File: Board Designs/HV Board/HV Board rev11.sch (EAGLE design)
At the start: 69 parts, among them IC1 OKI-78SR-5, IC2 NE5532SOIC

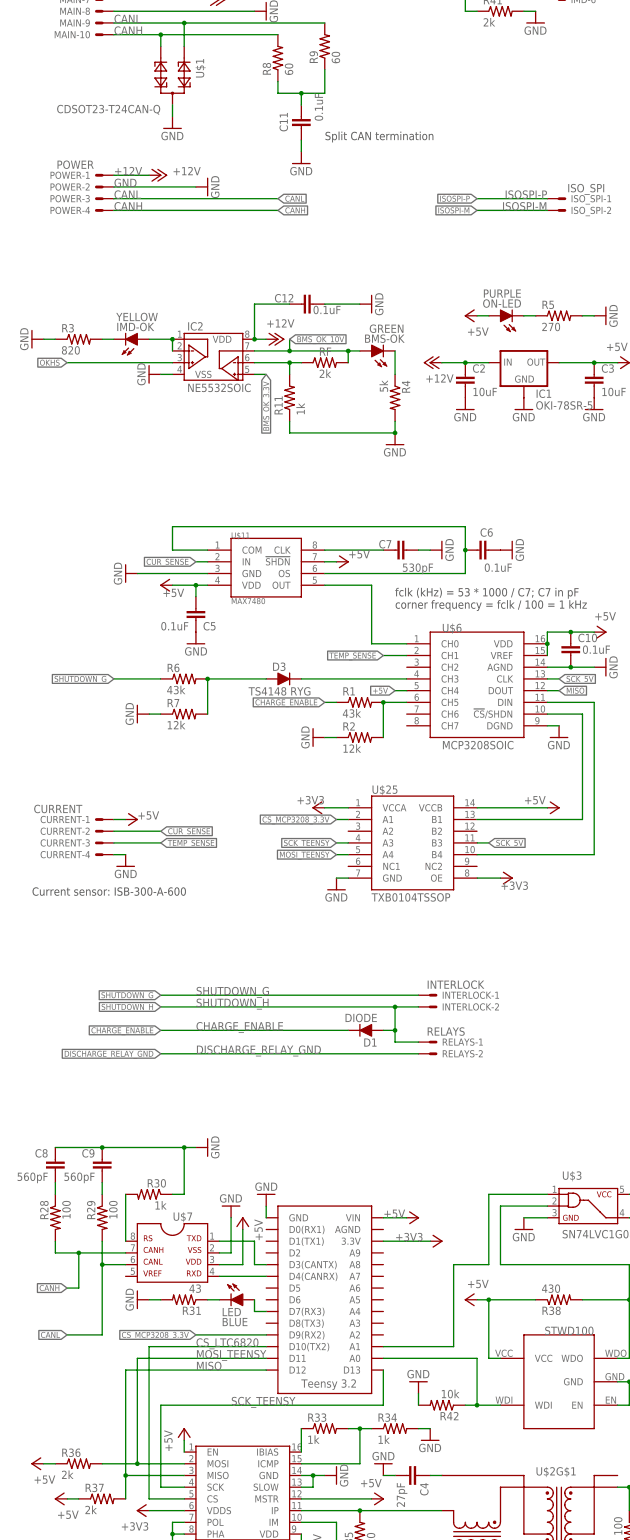
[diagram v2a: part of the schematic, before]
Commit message: HV Board: Added bypass caps to LTC6820 and SPI level shifter, rerouted under Teensy, rerouted GND/Power to 5V regulator, Silkscreen updates for mfg
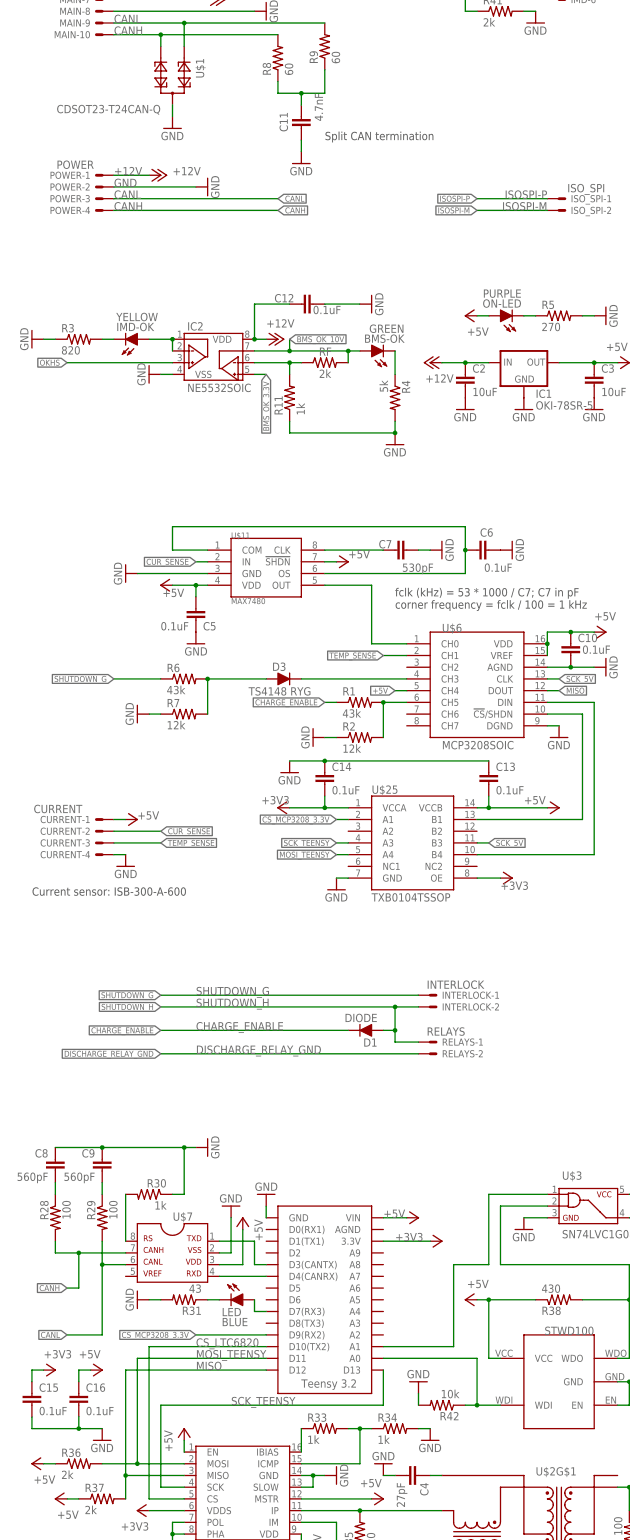
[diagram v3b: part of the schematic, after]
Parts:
- added C13, C14, C15, C16: 0.1uF, HyTechDevices:CAP0805
- C11: value 0.1uF -> 4.7nF
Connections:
- net +3V3: now also C14.1, C15.2
- net +5V: now also C13.1, C16.2
- net GND: now also C13.2, C14.2, C15.1, C16.1
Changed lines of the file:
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@@
 <part name="R8" library="HyTechDevices" deviceset="RESISTOR" device="0805-RES" value="60"/>
 <part name="R9" library="HyTechDevices" deviceset="RESISTOR" device="0805-RES" value="60"/>
-<part name="C11" library="HyTechDevices" deviceset="CAP" device="0805" value="0.1uF"/>
+<part name="C11" library="HyTechDevices" deviceset="CAP" device="0805" value="4.7nF"/>
 <part name="GND33" library="supply1" deviceset="GND" device=""/>
 <part name="RF" library="HyTechDevices" deviceset="RESISTOR" device="0805-RES" value="2k"/>
@@
 <part name="C12" library="HyTechDevices" deviceset="CAP" device="0805" value="0.1uF"/>
 <part name="GND34" library="supply1" deviceset="GND" device=""/>
+<part name="C13" library="HyTechDevices" deviceset="CAP" device="0805" value="0.1uF"/>
+<part name="C14" library="HyTechDevices" deviceset="CAP" device="0805" value="0.1uF"/>
+<part name="GND35" library="supply1" deviceset="GND" device=""/>
+<part name="C15" library="HyTechDevices" deviceset="CAP" device="0805" value="0.1uF"/>
+<part name="C16" library="HyTechDevices" deviceset="CAP" device="0805" value="0.1uF"/>
+<part name="GND36" library="HyTechSymbols" deviceset="GND" device=""/>
+<part name="P+9" library="supply1" deviceset="+5V" device=""/>
+<part name="+3V6" library="supply1" library_urn="urn:adsk.eagle:library:371" deviceset="+3V3" device=""/>
 </parts>
 <sheets>
@@
 <attribute name="VALUE" x="88.9" y="-160.02" size="1.778" layer="96"/>
 </instance>
-<instance part="+3V4" gate="G$1" x="76.2" y="-139.7" smashed="yes" rot="R90">
-<attribute name="VALUE" x="78.74" y="-137.16" size="1.778" layer="96" rot="R180"/>
+<instance part="+3V4" gate="G$1" x="68.58" y="-139.7" smashed="yes" rot="R90">
+<attribute name="VALUE" x="71.12" y="-137.16" size="1.778" layer="96" rot="R180"/>
 </instance>
 <instance part="+3V5" gate="G$1" x="119.38" y="-154.94" smashed="yes" rot="R270">
@@
 <instance part="GND34" gate="1" x="88.9" y="-30.48" smashed="yes" rot="R90">
 <attribute name="VALUE" x="91.44" y="-33.02" size="1.778" layer="96" rot="R90"/>
+</instance>
+<instance part="C13" gate="G$1" x="114.3" y="-132.08" smashed="yes" rot="MR180">
+<attribute name="NAME" x="115.824" y="-129.921" size="1.778" layer="95" rot="MR180"/>
+<attribute name="VALUE" x="115.824" y="-135.001" size="1.778" layer="96" rot="MR180"/>
+</instance>
+<instance part="C14" gate="G$1" x="78.74" y="-132.08" smashed="yes" rot="MR180">
+<attribute name="NAME" x="80.264" y="-129.921" size="1.778" layer="95" rot="MR180"/>
+<attribute name="VALUE" x="80.264" y="-135.001" size="1.778" layer="96" rot="MR180"/>
+</instance>
+<instance part="GND35" gate="1" x="71.12" y="-132.08" smashed="yes">
+<attribute name="VALUE" x="68.58" y="-134.62" size="1.778" layer="96"/>
+</instance>
+<instance part="C15" gate="G$1" x="15.24" y="-266.7" smashed="yes" rot="MR180">
+<attribute name="NAME" x="16.764" y="-264.541" size="1.778" layer="95" rot="MR180"/>
+<attribute name="VALUE" x="16.764" y="-269.621" size="1.778" layer="96" rot="MR180"/>
+</instance>
+<instance part="C16" gate="G$1" x="25.4" y="-266.7" smashed="yes" rot="MR180">
+<attribute name="NAME" x="26.924" y="-264.541" size="1.778" layer="95" rot="MR180"/>
+<attribute name="VALUE" x="26.924" y="-269.621" size="1.778" layer="96" rot="MR180"/>
+</instance>
+<instance part="GND36" gate="1" x="30.48" y="-276.86" smashed="yes">
+<attribute name="VALUE" x="27.94" y="-279.4" size="1.778" layer="96"/>
+</instance>
+<instance part="P+9" gate="1" x="30.48" y="-261.62" smashed="yes" rot="R270">
+<attribute name="VALUE" x="25.4" y="-259.08" size="1.778" layer="96"/>
+</instance>
+<instance part="+3V6" gate="G$1" x="20.32" y="-261.62" smashed="yes" rot="R270">
+<attribute name="VALUE" x="17.78" y="-259.08" size="1.778" layer="96"/>
 </instance>
 </instances>
@@
 <wire x1="78.74" y1="-30.48" x2="86.36" y2="-30.48" width="0.1524" layer="91"/>
 </segment>
+<segment>
+<pinref part="C13" gate="G$1" pin="2"/>
+<wire x1="114.3" y1="-129.54" x2="78.74" y2="-129.54" width="0.1524" layer="91"/>
+<pinref part="C14" gate="G$1" pin="2"/>
+<pinref part="GND35" gate="1" pin="GND"/>
+<wire x1="71.12" y1="-129.54" x2="78.74" y2="-129.54" width="0.1524" layer="91"/>
+<junction x="78.74" y="-129.54"/>
+</segment>
+<segment>
+<pinref part="C16" gate="G$1" pin="1"/>
+<wire x1="25.4" y1="-271.78" x2="25.4" y2="-274.32" width="0.1524" layer="91"/>
+<wire x1="25.4" y1="-274.32" x2="15.24" y2="-274.32" width="0.1524" layer="91"/>
+<pinref part="C15" gate="G$1" pin="1"/>
+<wire x1="15.24" y1="-274.32" x2="15.24" y2="-271.78" width="0.1524" layer="91"/>
+<junction x="25.4" y="-274.32"/>
+<pinref part="GND36" gate="1" pin="GND"/>
+<wire x1="30.48" y1="-274.32" x2="25.4" y2="-274.32" width="0.1524" layer="91"/>
+</segment>
 </net>
 <net name="+12V" class="0">
@@
 </segment>
 <segment>
-<wire x1="111.76" y1="-139.7" x2="127" y2="-139.7" width="0.1524" layer="91"/>
+<wire x1="111.76" y1="-139.7" x2="114.3" y2="-139.7" width="0.1524" layer="91"/>
 <pinref part="FLIP" gate="1" pin="+5V"/>
 <pinref part="U$25" gate="G$1" pin="VCCB"/>
+<pinref part="C13" gate="G$1" pin="1"/>
+<wire x1="114.3" y1="-139.7" x2="127" y2="-139.7" width="0.1524" layer="91"/>
+<wire x1="114.3" y1="-137.16" x2="114.3" y2="-139.7" width="0.1524" layer="91"/>
+<junction x="114.3" y="-139.7"/>
+</segment>
+<segment>
+<pinref part="P+9" gate="1" pin="+5V"/>
+<wire x1="27.94" y1="-261.62" x2="25.4" y2="-261.62" width="0.1524" layer="91"/>
+<pinref part="C16" gate="G$1" pin="2"/>
+<wire x1="25.4" y1="-261.62" x2="25.4" y2="-264.16" width="0.1524" layer="91"/>
 </segment>
 </net>
@@
 <pinref part="U$25" gate="G$1" pin="VCCA"/>
 <pinref part="+3V4" gate="G$1" pin="+3V3"/>
+<wire x1="71.12" y1="-139.7" x2="78.74" y2="-139.7" width="0.1524" layer="91"/>
+<pinref part="C14" gate="G$1" pin="1"/>
 <wire x1="78.74" y1="-139.7" x2="83.82" y2="-139.7" width="0.1524" layer="91"/>
+<wire x1="78.74" y1="-137.16" x2="78.74" y2="-139.7" width="0.1524" layer="91"/>
+<junction x="78.74" y="-139.7"/>
 </segment>
 <segment>
@@
 <wire x1="116.84" y1="-154.94" x2="111.76" y2="-154.94" width="0.1524" layer="91"/>
 </segment>
-</net>
+<segment>
+<pinref part="+3V6" gate="G$1" pin="+3V3"/>
+<wire x1="17.78" y1="-261.62" x2="15.24" y2="-261.62" width="0.1524" layer="91"/>
+<pinref part="C15" gate="G$1" pin="2"/>
+<wire x1="15.24" y1="-261.62" x2="15.24" y2="-264.16" width="0.1524" layer="91"/>
+</segment>
+</net>

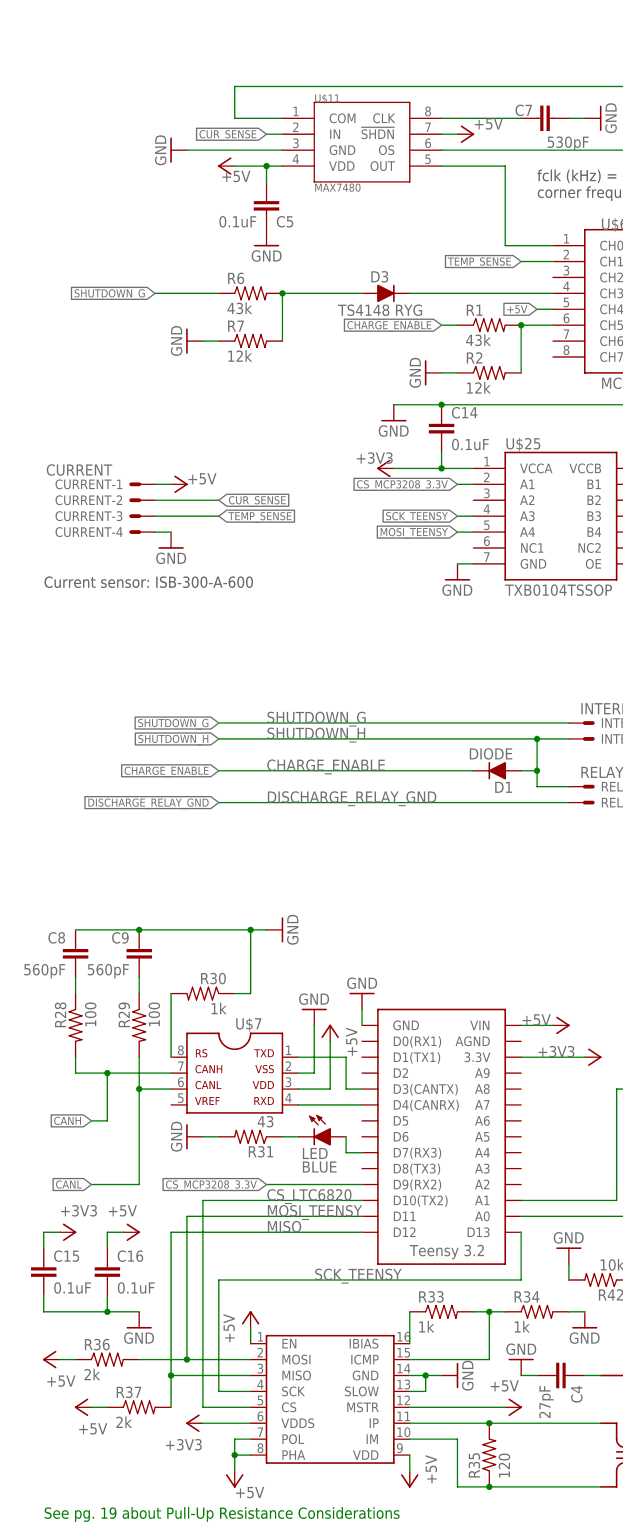
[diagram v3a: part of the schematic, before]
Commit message: Final version of HV board rev11 sent for mfg
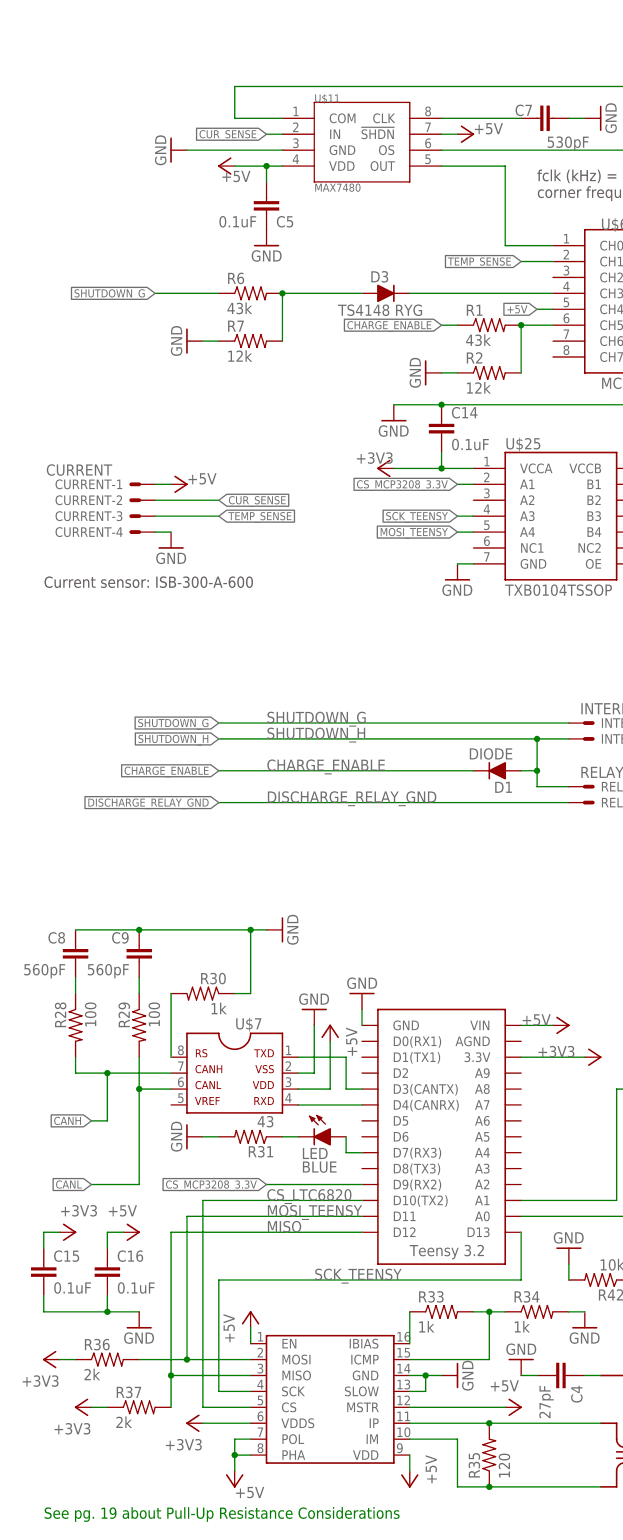
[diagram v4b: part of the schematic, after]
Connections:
- removed net N$8: U$11.!SHDN
- net +3V3: now also R36.1, R37.1
- net +5V: now also U$11.!SHDN; no longer R36.1, R37.1
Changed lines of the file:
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@@
 <part name="R36" library="HyTechDevices" deviceset="RESISTOR" device="0805-RES" value="2k"/>
 <part name="R37" library="HyTechDevices" deviceset="RESISTOR" device="0805-RES" value="2k"/>
-<part name="P+19" library="supply1" deviceset="+5V" device=""/>
-<part name="P+20" library="supply1" deviceset="+5V" device=""/>
 <part name="U$9" library="HyTechDevices" deviceset="TEENSY_3.2_SIMPLE" device=""/>
 <part name="GND24" library="supply1" library_urn="urn:adsk.eagle:library:371" deviceset="GND" device=""/>
@@
 <part name="GND9" library="supply1" deviceset="GND" device=""/>
 <part name="P+3" library="supply1" deviceset="+5V" device=""/>
-<part name="P+5" library="supply1" deviceset="+5V" device=""/>
 <part name="GND2" library="supply1" deviceset="GND" device=""/>
 <part name="C5" library="HyTechDevices" deviceset="CAP" device="0805" value="0.1uF"/>
@@
 <part name="P+9" library="supply1" deviceset="+5V" device=""/>
 <part name="+3V6" library="supply1" library_urn="urn:adsk.eagle:library:371" deviceset="+3V3" device=""/>
+<part name="+3V7" library="supply1" library_urn="urn:adsk.eagle:library:371" deviceset="+3V3" device=""/>
+<part name="+3V8" library="supply1" library_urn="urn:adsk.eagle:library:371" deviceset="+3V3" device=""/>
+<part name="P+5" library="supply1" deviceset="+5V" device=""/>
 </parts>
 <sheets>
@@
 <attribute name="VALUE" x="26.67" y="-292.862" size="1.778" layer="96"/>
 </instance>
-<instance part="P+19" gate="1" x="15.24" y="-281.94" smashed="yes" rot="R90">
-<attribute name="VALUE" x="20.32" y="-284.48" size="1.778" layer="96" rot="R180"/>
-</instance>
-<instance part="P+20" gate="1" x="20.32" y="-289.56" smashed="yes" rot="R90">
-<attribute name="VALUE" x="25.4" y="-292.1" size="1.778" layer="96" rot="R180"/>
-</instance>
 <instance part="U$9" gate="G$1" x="68.58" y="-266.7" smashed="yes"/>
 <instance part="GND24" gate="1" x="66.04" y="-223.52" smashed="yes" rot="R180">
@@
 <instance part="P+3" gate="1" x="43.18" y="-91.44" smashed="yes" rot="MR270">
 <attribute name="VALUE" x="48.26" y="-93.98" size="1.778" layer="96" rot="MR0"/>
-</instance>
-<instance part="P+5" gate="1" x="83.82" y="-86.36" smashed="yes" rot="MR90">
-<attribute name="VALUE" x="83.82" y="-83.82" size="1.778" layer="96" rot="MR180"/>
 </instance>
 <instance part="GND2" gate="1" x="35.56" y="-88.9" smashed="yes" rot="MR90">
@@
 <instance part="+3V6" gate="G$1" x="20.32" y="-261.62" smashed="yes" rot="R270">
 <attribute name="VALUE" x="17.78" y="-259.08" size="1.778" layer="96"/>
+</instance>
+<instance part="+3V7" gate="G$1" x="20.32" y="-289.56" smashed="yes" rot="R90">
+<attribute name="VALUE" x="22.86" y="-292.1" size="1.778" layer="96" rot="R180"/>
+</instance>
+<instance part="+3V8" gate="G$1" x="15.24" y="-281.94" smashed="yes" rot="R90">
+<attribute name="VALUE" x="17.78" y="-284.48" size="1.778" layer="96" rot="R180"/>
+</instance>
+<instance part="P+5" gate="1" x="83.82" y="-86.36" smashed="yes" rot="R270">
+<attribute name="VALUE" x="83.82" y="-86.36" size="1.778" layer="96"/>
 </instance>
 </instances>
@@
 </segment>
 <segment>
-<pinref part="R36" gate="G$1" pin="1"/>
-<pinref part="P+19" gate="1" pin="+5V"/>
-<wire x1="17.78" y1="-281.94" x2="20.32" y2="-281.94" width="0.1524" layer="91"/>
-</segment>
-<segment>
-<pinref part="R37" gate="G$1" pin="1"/>
-<pinref part="P+20" gate="1" pin="+5V"/>
-<wire x1="22.86" y1="-289.56" x2="25.4" y2="-289.56" width="0.1524" layer="91"/>
-</segment>
-<segment>
 <pinref part="U$8" gate="G$1" pin="MSTR"/>
 <wire x1="73.66" y1="-289.56" x2="88.9" y2="-289.56" width="0.1524" layer="91"/>
@@
 <pinref part="C16" gate="G$1" pin="2"/>
 <wire x1="25.4" y1="-261.62" x2="25.4" y2="-264.16" width="0.1524" layer="91"/>
+</segment>
+<segment>
+<wire x1="81.28" y1="-86.36" x2="78.74" y2="-86.36" width="0.1524" layer="91"/>
+<pinref part="U$11" gate="G$1" pin="!SHDN"/>
+<pinref part="P+5" gate="1" pin="+5V"/>
 </segment>
 </net>
@@
 <pinref part="C15" gate="G$1" pin="2"/>
 <wire x1="15.24" y1="-261.62" x2="15.24" y2="-264.16" width="0.1524" layer="91"/>
+</segment>
+<segment>
+<pinref part="R37" gate="G$1" pin="1"/>
+<wire x1="22.86" y1="-289.56" x2="25.4" y2="-289.56" width="0.1524" layer="91"/>
+<pinref part="+3V7" gate="G$1" pin="+3V3"/>
+</segment>
+<segment>
+<pinref part="R36" gate="G$1" pin="1"/>
+<wire x1="17.78" y1="-281.94" x2="20.32" y2="-281.94" width="0.1524" layer="91"/>
+<pinref part="+3V8" gate="G$1" pin="+3V3"/>
 </segment>
 </net>
@@
 </segment>
 </net>
-<net name="N$8" class="0">
-<segment>
-<pinref part="P+5" gate="1" pin="+5V"/>
-<wire x1="81.28" y1="-86.36" x2="78.74" y2="-86.36" width="0.1524" layer="91"/>
-<pinref part="U$11" gate="G$1" pin="!SHDN"/>
-</segment>
-</net>
